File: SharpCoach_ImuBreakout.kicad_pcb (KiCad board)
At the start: 2 copper layers, 24.6 x 21.8 mm, 10 parts, among them J1 INTERFACE, U1 LIS3DH, U2 BMG250

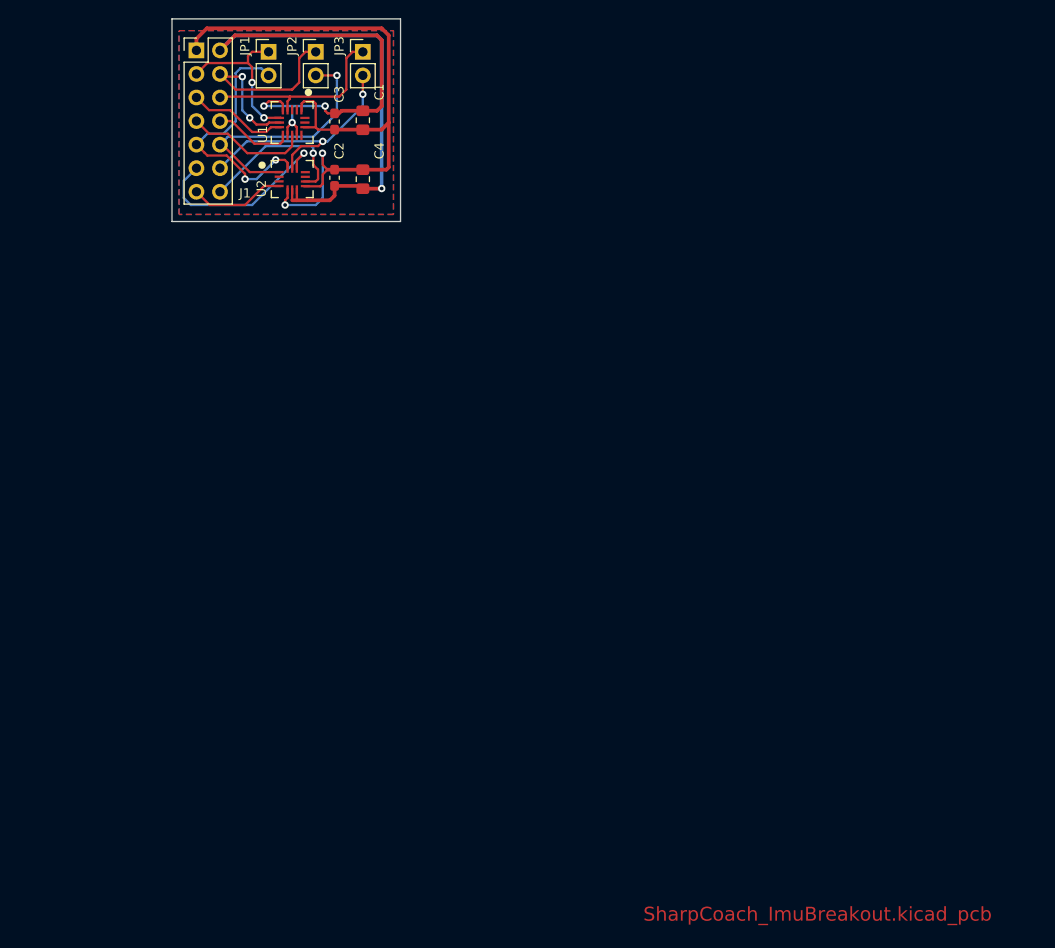
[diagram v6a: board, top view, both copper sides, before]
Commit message: Updated silkscreen with pinout
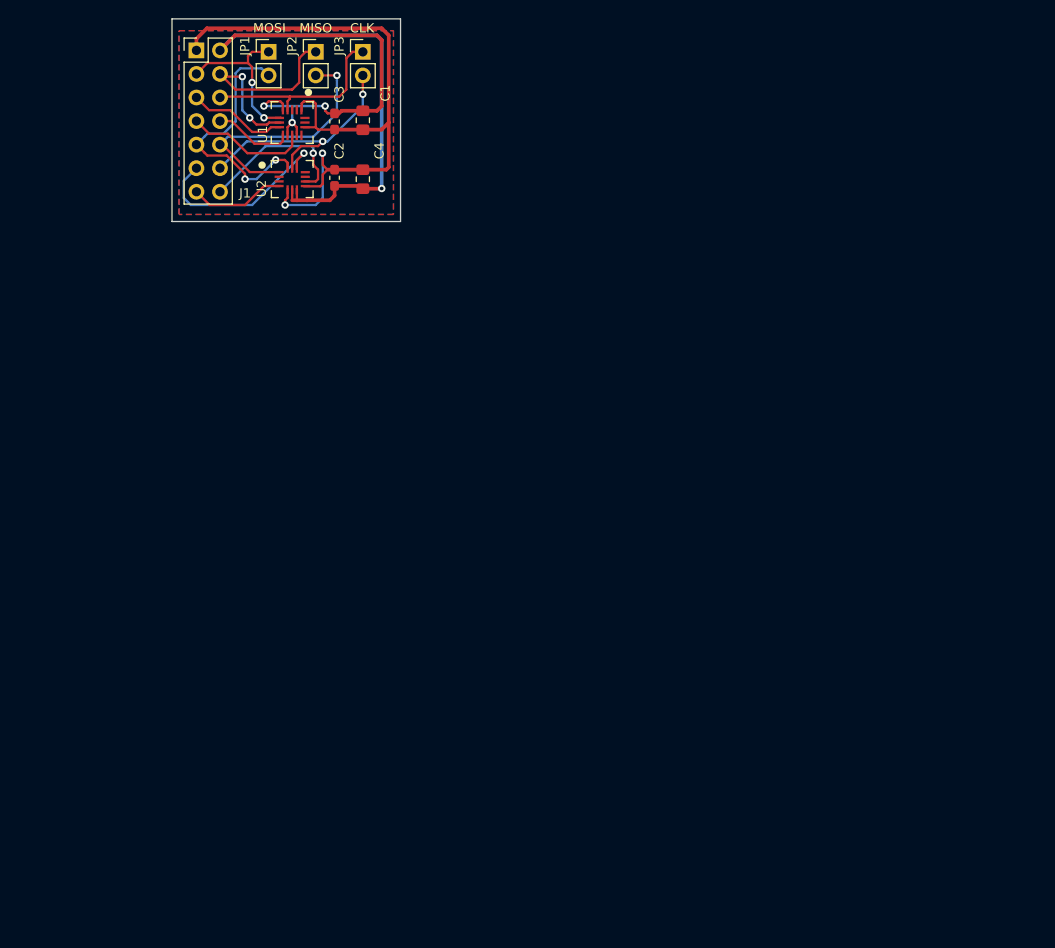
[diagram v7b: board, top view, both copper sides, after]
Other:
- board text added: "CLK"
- board text added: "GND MISO_AC CLK_AC INT2_AC MISO_GY CLK_GY INT2_GY"
- board text added: "MISO"
- board text added: "MOSI"
- board text added: "VIN MOSI_AC CS_AC INT1_AC MOSI_GY CS_GY INT1_GY"
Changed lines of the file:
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@@
-(kicad_pcb (version 20171130) (host pcbnew "(5.0.0)")
+(kicad_pcb (version 20171130) (host pcbnew 5.0.0-fee4fd1~66~ubuntu16.04.1)
   (general
     (thickness 1.6)
-    (drawings 10)
+    (drawings 15)
     (tracks 209)
     (zones 0)
@@
     (0 F.Cu signal)
     (31 B.Cu signal)
-    (32 B.Adhes user)
-    (33 F.Adhes user)
+    (32 B.Adhes user hide)
+    (33 F.Adhes user hide)
     (34 B.Paste user)
     (35 F.Paste user)
@@
     (37 F.SilkS user)
     (38 B.Mask user)
-    (39 F.Mask user)
+    (39 F.Mask user hide)
     (40 Dwgs.User user)
     (41 Cmts.User user)
@@
     (tags "capacitor handsolder")
     (attr smd)
-    (fp_text reference C1 (at 3.057 1.778 90) (layer F.SilkS)
+    (fp_text reference C1 (at 2.931 2.426 90) (layer F.SilkS)
       (effects (font (size 1 1) (thickness 0.15)))
     )
@@
     )
   )
-  (gr_text SharpCoach_ImuBreakout.kicad_pcb (at 203.962 185.674) (layer F.Cu)
+  (gr_text CLK (at 154.866 90.154) (layer F.SilkS)
+    (effects (font (size 1 1) (thickness 0.15)))
+  )
+  (gr_text MISO (at 149.866 90.154) (layer F.SilkS)
+    (effects (font (size 1 1) (thickness 0.15)))
+  )
+  (gr_text MOSI (at 144.866 90.154) (layer F.SilkS)
+    (effects (font (size 1 1) (thickness 0.15)))
+  )
+  (gr_text "GND\nMISO_AC\nCLK_AC\nINT2_AC\nMISO_GY\nCLK_GY\nINT2_GY" (at 158.366 103.654) (layer B.SilkS)
+    (effects (font (size 1 1) (thickness 0.15)) (justify left mirror))
+  )
+  (gr_text "VIN\nMOSI_AC\nCS_AC\nINT1_AC\nMOSI_GY\nCS_GY\nINT1_GY" (at 148.866 103.654) (layer B.SilkS)
+    (effects (font (size 1 1) (thickness 0.15)) (justify left mirror))
+  )
+  (gr_text SharpCoach_ImuBreakout.kicad_pcb (at 203.962 185.674) (layer Dwgs.User)
     (effects (font (size 1.5 1.5) (thickness 0.15)))
   )

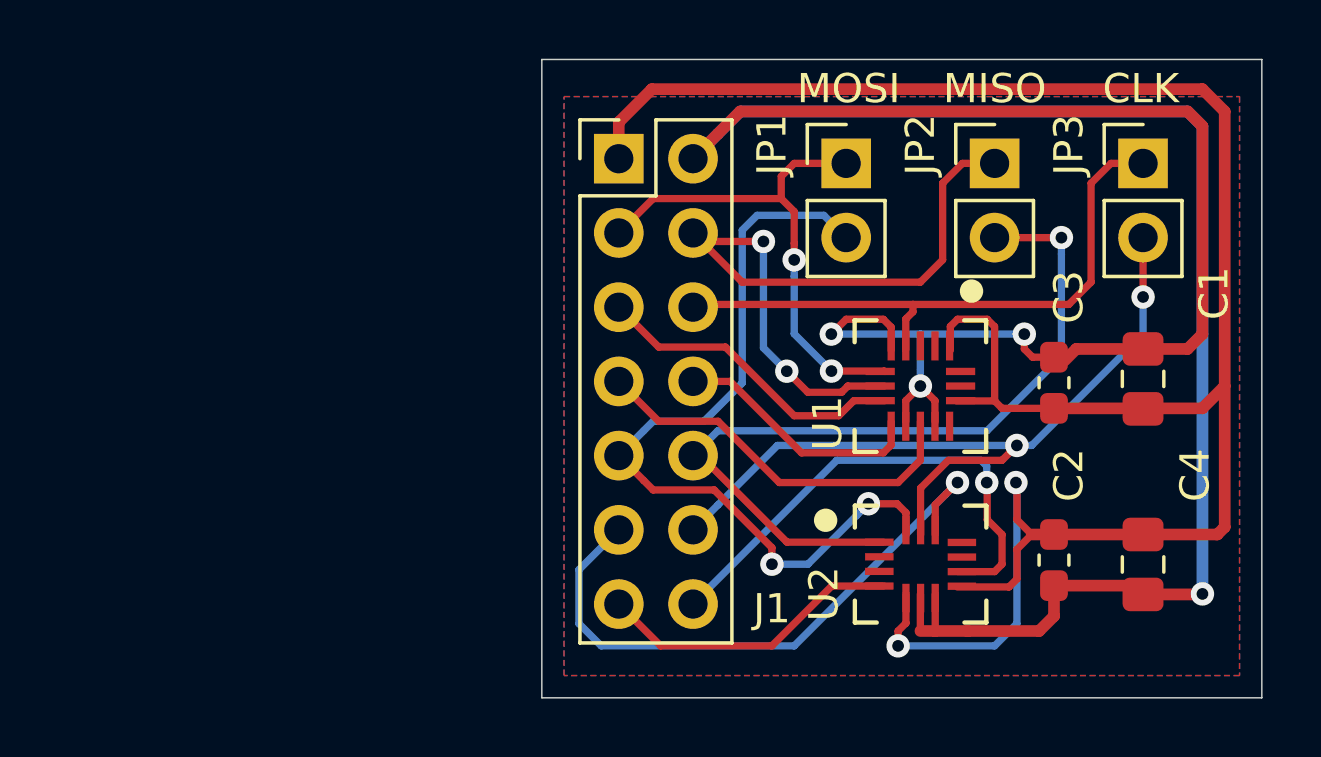
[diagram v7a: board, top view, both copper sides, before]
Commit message: Updated library paths to use submodules.
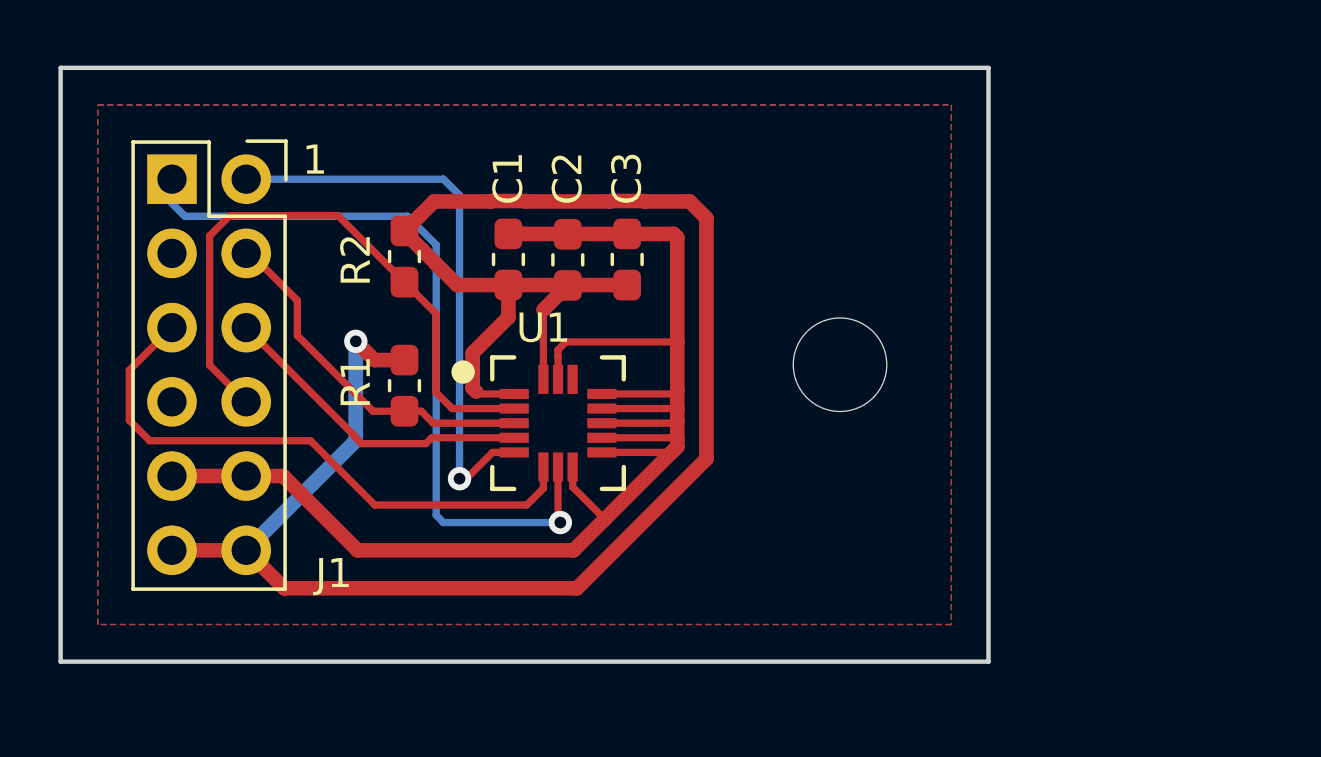
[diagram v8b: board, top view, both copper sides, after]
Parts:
- removed C4: 10u, Capacitor_SMD:C_0805_2012Metric_Pad1.15x1.40mm_HandSolder
- removed JP1: Jumper SPI MOSI, Connector_PinHeader_2.54mm:PinHeader_1x02_P2.54mm_Vertical
- removed JP2: Jumper SPI MISO, Connector_PinHeader_2.54mm:PinHeader_1x02_P2.54mm_Vertical
- removed JP3: Jumper SPI CLK, Connector_PinHeader_2.54mm:PinHeader_1x02_P2.54mm_Vertical
- removed U2: BMG250, BMG250:BMG250
- added R1: 10k, Resistor_SMD:R_0603_1608Metric_Pad1.05x0.95mm_HandSolder, F.Cu at (129.7, 100.3)
- added R2: 10k, Resistor_SMD:R_0603_1608Metric_Pad1.05x0.95mm_HandSolder, F.Cu at (129.7, 95.9)
- added REF**: MountingHole_3.2mm_M3, MountingHole:MountingHole_3.2mm_M3, F.Cu at (144.6, 99.6)
- C1: value 10u -> 100n; footprint Capacitor_SMD:C_0805_2012Metric_Pad1.15x1.40mm_HandSolder -> Capacitor_SMD:C_0603_1608Metric_Pad1.05x0.95mm_HandSolder
- C3: value 100n -> 1u
- J1: value INTERFACE -> PMOD_Type2A_Variant01; footprint Connector_PinHeader_2.54mm:PinHeader_2x07_P2.54mm_Vertical -> PMOD_SpecB:PMOD_SpecB
- U1: value LIS3DH -> LSM6DS33; footprint LIS3DH:LIS3DH -> LSM6DS33:LSM6DS33
- moved C1 22.1 mm to (133.2, 96.0)
- moved C2 19.6 mm to (135.3, 96.0), turned to 90 degrees
- moved C3 15.2 mm to (137.3, 96.0)
- moved J1 12.8 mm to (124.2, 93.2)
- moved U1 12.5 mm to (134.9, 101.6), turned to 0 degrees
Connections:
- J1 pad 1: +3V3 -> /SS
- J1 pad 10: /MISO_GYRO -> Net-(J1-Pad10)
- J1 pad 11: /CS_GYRO -> GND
- J1 pad 12: /CLK_GYRO -> +3V3
- J1 pad 2: GND -> /MOSI
- J1 pad 3: /MOSI_ACCEL -> /MISO
- J1 pad 4: /MISO_ACCEL -> /SCK
- J1 pad 5: /CS_ACCEL -> GND
- J1 pad 6: /CLK_ACCEL -> +3V3
- J1 pad 7: /INT1_ACCEL -> /INT1
- J1 pad 8: /INT2_ACCEL -> Net-(J1-Pad8)
- J1 pad 9: /MOSI_GYRO -> /INT2
- U1 pad 11: /INT1_ACCEL -> GND
- U1 pad 13: Net-(U1-Pad13) -> GND
- U1 pad 14: +3V3 -> Net-(U1-Pad14)
- U1 pad 15: Net-(U1-Pad15) -> GND
- U1 pad 16: Net-(U1-Pad16) -> +3V3
- U1 pad 2: Net-(U1-Pad2) -> /SCK
- U1 pad 3: Net-(U1-Pad3) -> /MOSI
- U1 pad 4: /CLK_ACCEL -> /MISO
- U1 pad 5: GND -> /SS
- U1 pad 6: /MOSI_ACCEL -> /INT2
- U1 pad 7: /MISO_ACCEL -> /INT1
- U1 pad 8: /CS_ACCEL -> GND
- U1 pad 9: /INT2_ACCEL -> GND
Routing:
- net GND: track 94.5 -> 54.4 mm, vias 4 -> 0
- net /MISO_GYRO: track 28.1 -> 0.00 mm, vias 1 -> 0
- net /MOSI_GYRO: track 28.0 -> 0.00 mm, vias 2 -> 0
- net /CLK_GYRO: track 27.2 -> 0.00 mm, vias 2 -> 0
- net /INT1: track 0.00 -> 26.1 mm, vias 0 -> 1
- net /MISO_ACCEL: track 25.3 -> 0.00 mm, vias 2 -> 0
- net /SCK: track 0.00 -> 21.5 mm
- net /CS_GYRO: track 21.5 -> 0.00 mm, vias 1 -> 0
- net /CLK_ACCEL: track 21.1 -> 0.00 mm
- net /INT2: track 0.00 -> 20.3 mm
- net /SS: track 0.00 -> 19.6 mm, vias 0 -> 1
- net /MOSI_ACCEL: track 17.6 -> 0.00 mm, vias 2 -> 0
- net /INT2_GYRO: track 17.1 -> 0.00 mm, vias 1 -> 0
- net /INT1_ACCEL: track 13.4 -> 0.00 mm
- net /MOSI: track 0.00 -> 12.4 mm
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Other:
- board size 24.6 x 21.8 mm -> 31.8 x 20.3 mm
- net class Power: trace_width 0.4 -> 0.5
- net class Signal added: clearance 0.2, trace_width 0.25, via_dia 0.8, via_drill 0.4
- rule pad_to_mask_clearance: 0.0508 -> 0.15
- board text added: "SharpCoach IMU breakout v1.0 Kamil Rogozinski 2019 CC BY-SA 4.0"
- board text removed: "CLK"
- board text removed: "GND MISO_AC CLK_AC INT2_AC MISO_GY CLK_GY INT2_GY"
- board text removed: "MISO"
- board text removed: "MOSI"
- board text removed: "SharpCoach IMU Breakout v1 Kamil Rogozinski CC BY-SA 4.0"
- board text removed: "SharpCoach_ImuBreakout.kicad_pcb"
- board text removed: "VIN MOSI_AC CS_AC INT1_AC MOSI_GY CS_GY INT1_GY"
